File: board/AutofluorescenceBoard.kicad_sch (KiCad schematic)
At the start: 41 parts, among them J1 2002411212, Q1 BSS138, U1 PAM2863ECR, U2 PAM2863ECR, U3 PAM2863ECR

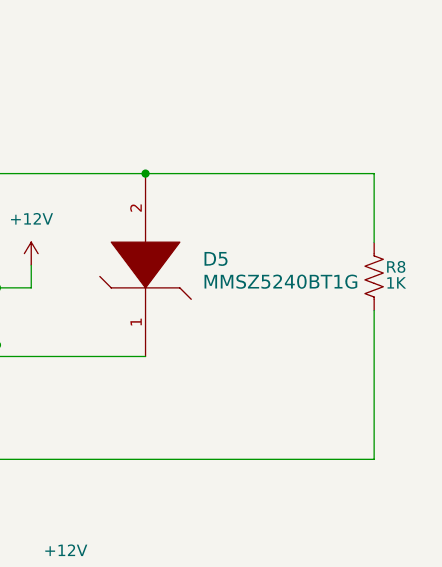
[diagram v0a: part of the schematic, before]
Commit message: Changed Resistors and Board/Mounting Hole Dimensions
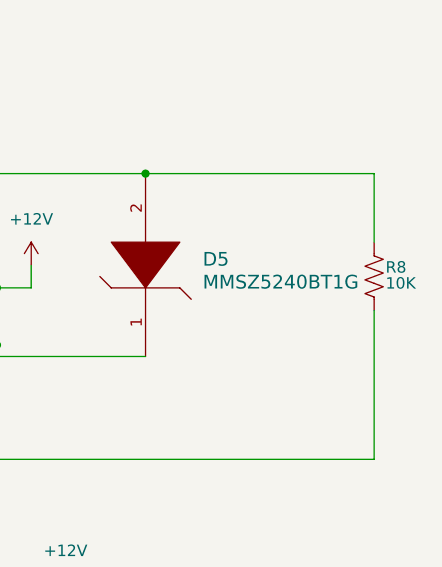
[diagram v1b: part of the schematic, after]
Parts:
- R8: value 1K -> 10K

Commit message: Layout Changes from CDR
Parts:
- R3: value 0.3 -> 0.15

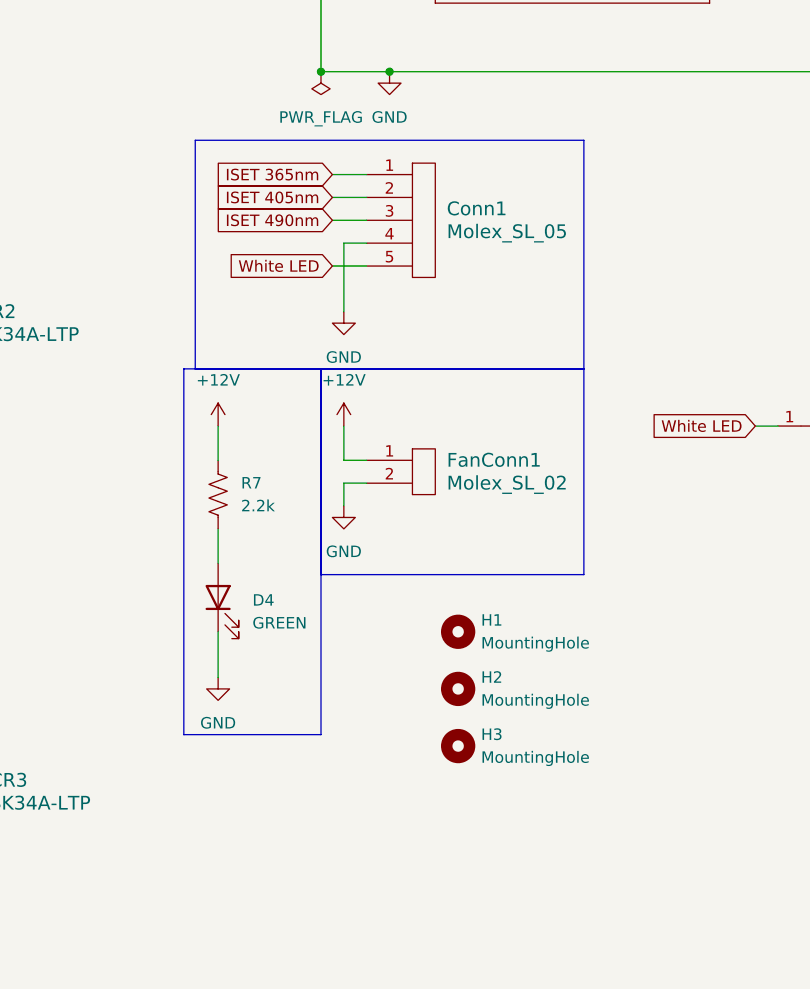
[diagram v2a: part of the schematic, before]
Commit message: Confined leds white and UV to .25 in radius
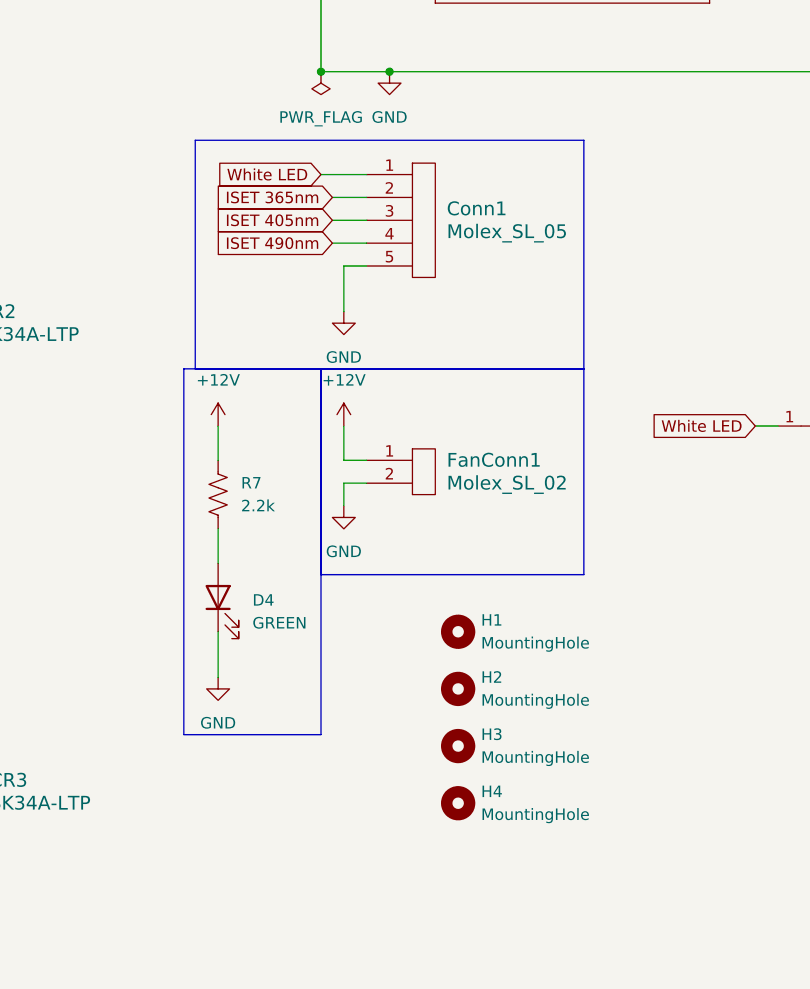
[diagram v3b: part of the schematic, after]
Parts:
- added H4: MountingHole, MRDT_Drill_Holes:6_32_Hole_Corner, symbol Mechanical:MountingHole
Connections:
- net GND: now also Conn1.5; no longer Conn1.4
- net ISET 365nm: now also Conn1.2; no longer Conn1.1
- net ISET 405nm: now also Conn1.3; no longer Conn1.2
- net ISET 490nm: now also Conn1.4; no longer Conn1.3
- net White LED: now also Conn1.1; no longer Conn1.5

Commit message: Rev2 Initial Component Placement
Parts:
- added R10: 10K, Resistor_SMD:R_0603_1608Metric_Pad0.98x0.95mm_HandSolder, symbol Device:R_US
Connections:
- net GND: now also R10.2
- net White LED: now also R10.1

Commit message: Fixed Errror
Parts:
- removed TP1, TP2, TP3: TestPoint, TestPoint:TestPoint_Pad_D1.5mm, symbol Connector:TestPoint
- CR1, CR2, CR3: footprint SMADO-214AC_MCC -> AutofluorescenceBoard:SMADO-214AC_MCC
- H1, H2, H3, H4: footprint MRDT_Drill_Holes:6_32_Hole_Corner -> MountingHole:MountingHole_2.2mm_M2
- U1, U2, U3: footprint SOIC_863ECR_DIO -> PAM2863ECR:SOIC_863ECR_DIO

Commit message: Fixed Footprint for Zener Diode
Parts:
- D5: footprint MRDT_Devices:SOD-123_ONS-L -> AutofluorescenceBoard:DIO_MMSZ5221BT1G

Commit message: Screwed Up MRDT Library on Laptop
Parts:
- Conn1: footprint AutofluorescenceBoard:MOLEX_SL_05_Vertical_AF -> MRDT_Connectors:MOLEX_SL_05_Horizontal
- FanConn1: footprint AutofluorescenceBoard:MOLEX_SL_02_Horizontal -> MRDT_Connectors:MOLEX_SL_02_Horizontal
- H1, H2, H3, H4: footprint MountingHole:MountingHole_2.2mm_M2 -> MRDT_Drill_Holes:M2_Hole
- J1: footprint AutofluorescenceBoard:CONN_SD-172286-1000_02_MOL -> MRDT_Connectors:MOLEX_SL_02_Horizontal

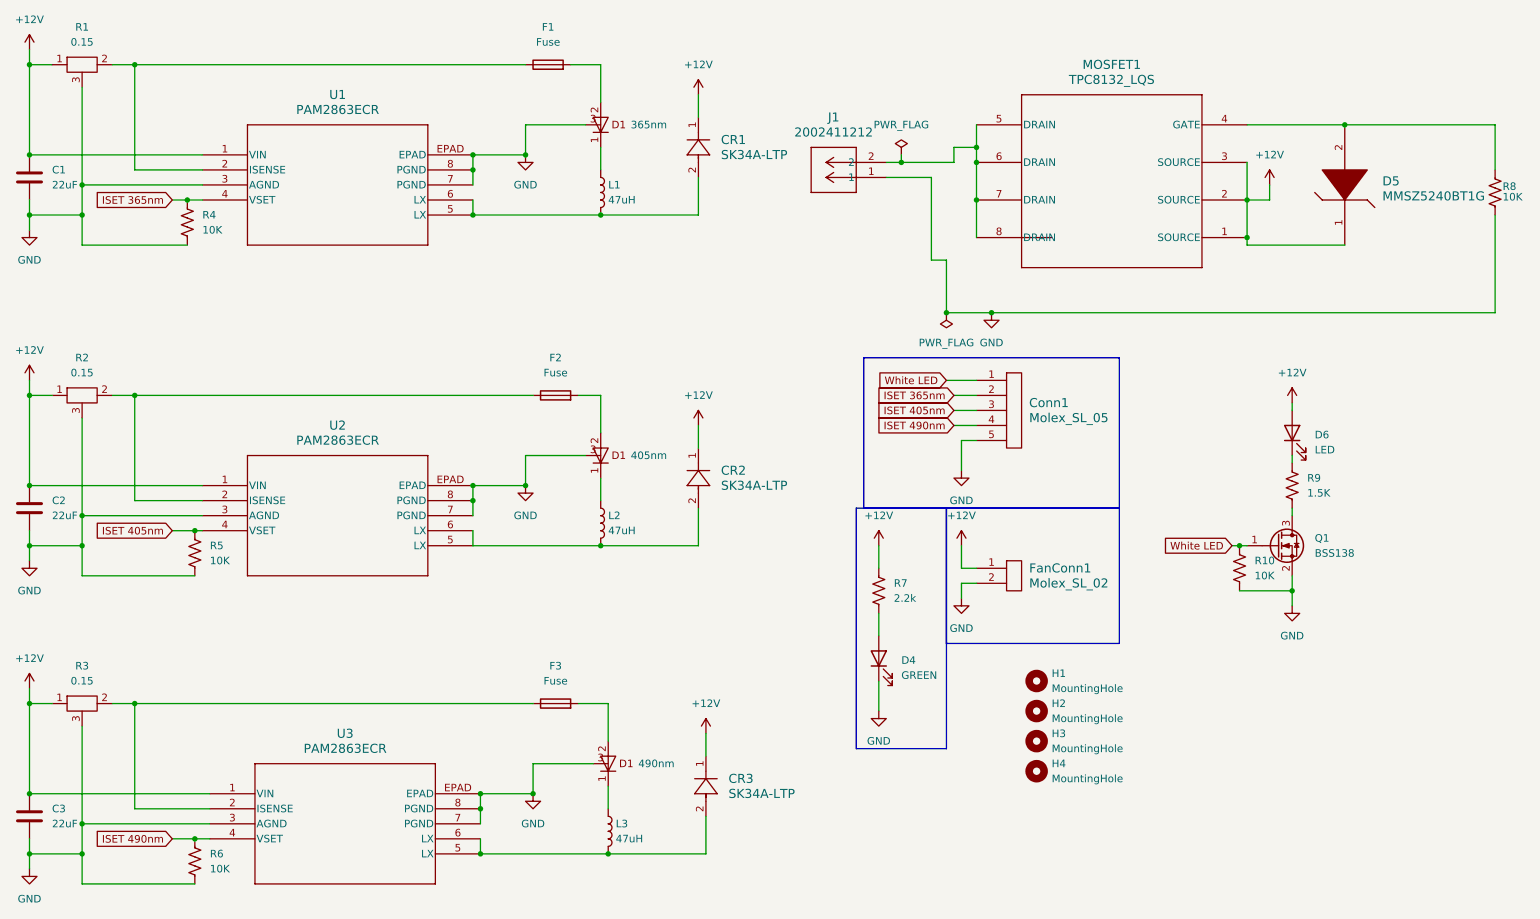
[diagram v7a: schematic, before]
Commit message: Updated Schematic, Mounting Holes, and a couple 3D models
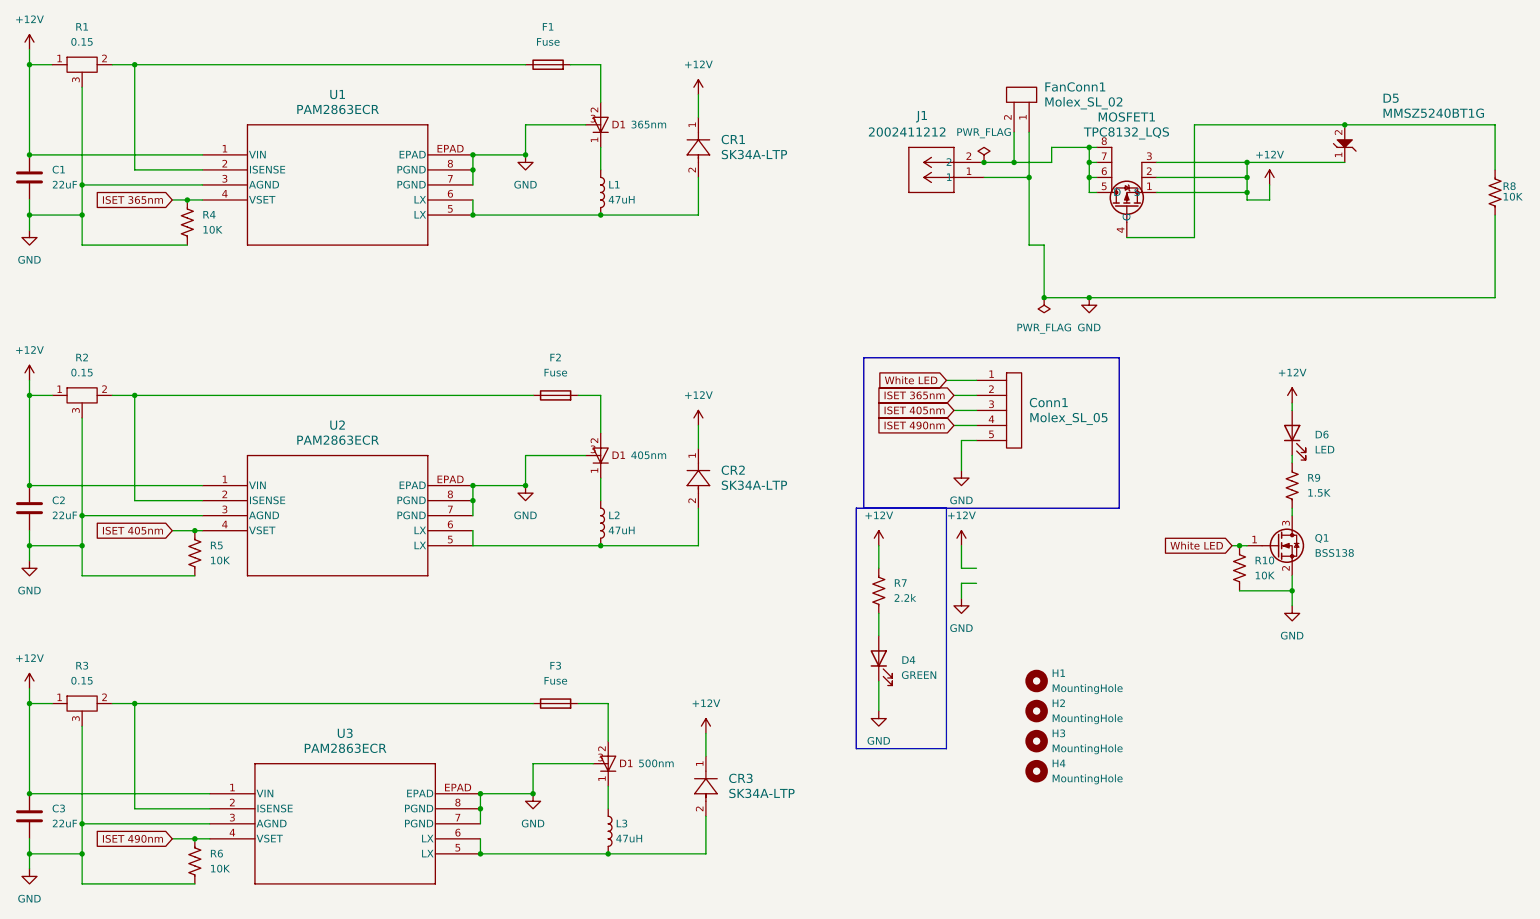
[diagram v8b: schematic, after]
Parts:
- D3: value 490nm -> 500nm
- D5: footprint AutofluorescenceBoard:DIO_MMSZ5221BT1G -> MRDT_Devices:SOD-123_ONS-L
- MOSFET1: footprint MRDT_Devices:SOP-8_TOS-L -> Package_SO:SOIC-8_3.9x4.9mm_P1.27mm
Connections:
- net +12V: no longer FanConn1.1
- net GND: now also FanConn1.1; no longer FanConn1.2
- net at J1.2, MOSFET1.5 (D), MOSFET1.6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: now also FanConn1.2
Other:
- moved on the sheet: D5, FanConn1, J1
